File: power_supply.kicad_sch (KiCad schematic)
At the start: 41 parts, among them J1 CONN_01X01, J2 CONN_01X01, J3 CONN_01X01, J4 CONN_01X01, Q1 MMBT42, Q2 FDS2672CT, U1 UCC3803

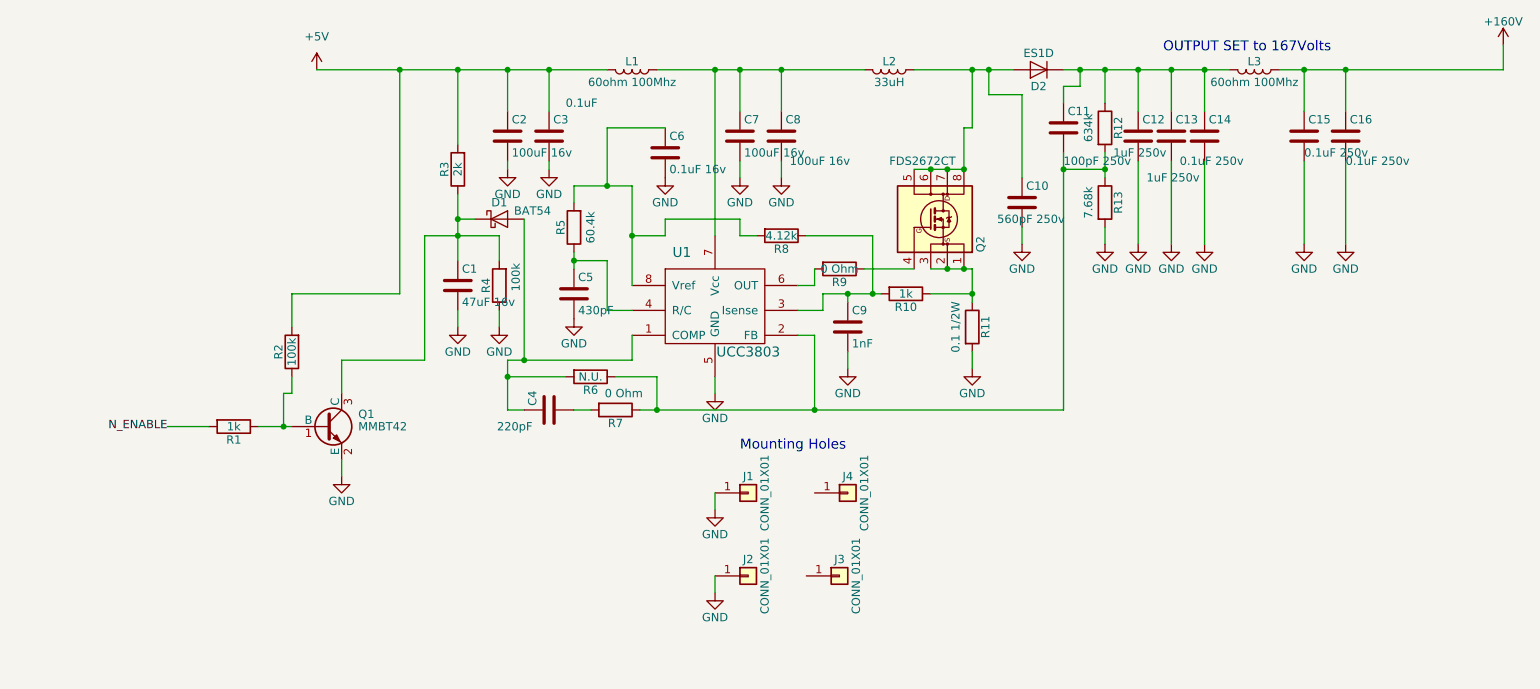
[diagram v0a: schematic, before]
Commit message: Update power supply layout and add associated components
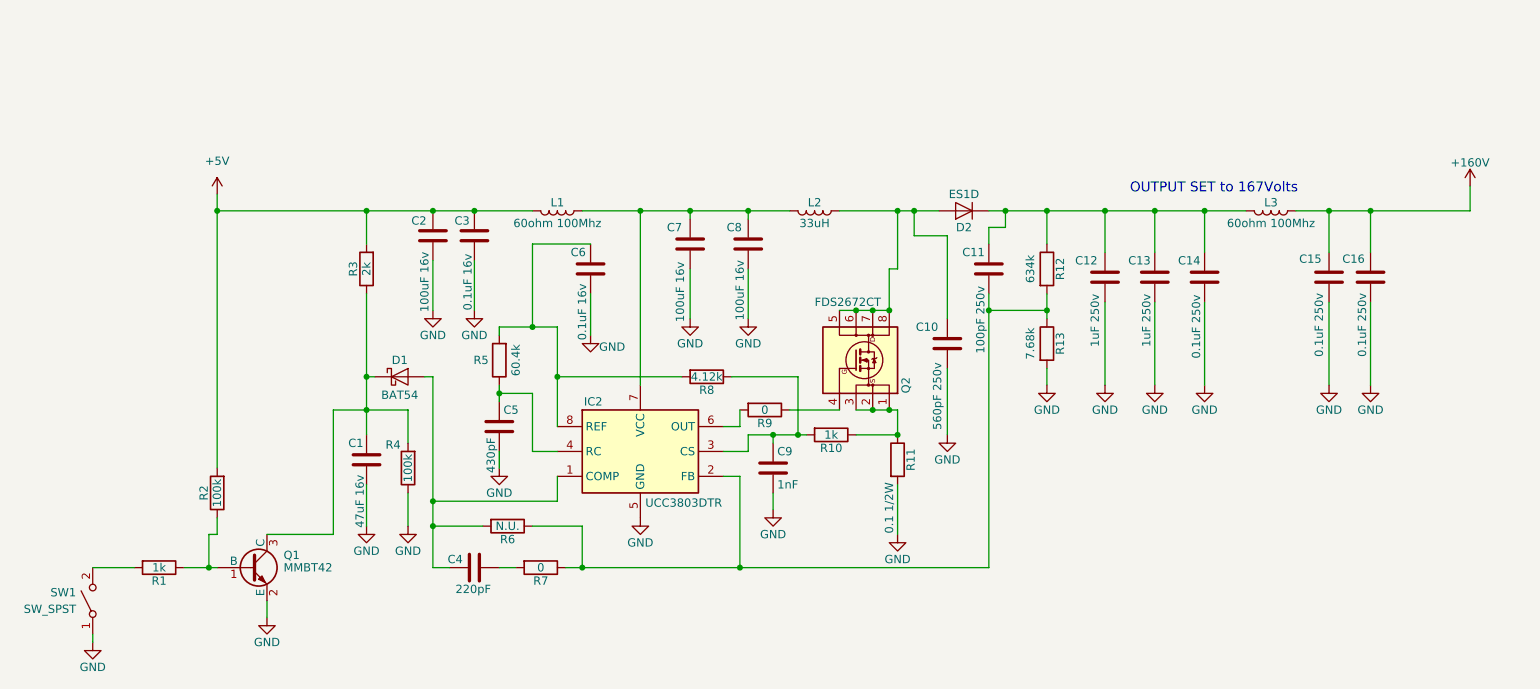
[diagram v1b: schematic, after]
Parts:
- removed J1, J2: CONN_01X01, MountingHole:MountingHole_2.2mm_M2_Pad, symbol NixieSupply5vto160vDCMBoost-rescue:Conn_01x01
- removed J3, J4: CONN_01X01, MountingHole:MountingHole_2.2mm_M2, symbol NixieSupply5vto160vDCMBoost-rescue:Conn_01x01
- removed U1: UCC3803, Package_SO:SOIC-8-1EP_3.9x4.9mm_P1.27mm_EP2.29x3mm, symbol NixieSupply5vto160vDCMBoost-rescue:AAC243
- added IC2: UCC3803DTR, eclectronics_nixie_footprints:SOIC127P600X175-8N, symbol eclectronics_nixie_lib:UCC3803DTR Buck Converter Controller
- added SW1: SW_SPST, symbol Switch:SW_SPST
- C3: value 0.1uF -> 0.1uF 16v
- D1: DigikeyPN (none) -> BAT54HT1GOSCT-ND; LCSCPN (none) -> C7422626; MFN (none) -> onsemi; MPN BAT54WS-7-F -> BAT54HT1G
- D2: DigikeyPN (none) -> ES1DFSCT-ND; MFN (none) -> onsemi
- L1: footprint Resistor_SMD:R_0805_2012Metric_Pad1.20x1.40mm_HandSolder -> Inductor_SMD:L_0805_2012Metric; MFN (none) -> Bourns Inc.; MPN BKP2125HS600-T -> MH2029-600Y
- L2: DigikeyPN (none) -> 732-1244-1-ND; MFN (none) -> Würth Elektronik
- L3: footprint Resistor_SMD:R_0805_2012Metric_Pad1.20x1.40mm_HandSolder -> Inductor_SMD:L_0805_2012Metric; MFN (none) -> Bourns Inc.; MPN (none) -> MH2029-600Y
- R7, R9: value 0 Ohm -> 0
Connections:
- net GND: now also IC2.5 (GND), SW1.1 (A)
- net at C7.1, C8.1, L1.1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: now also IC2.7 (VCC)
- net at C11.2, R12.2, R13.1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: now also IC2.2 (FB)
- net at C5.1, R5.1: now also IC2.4 (RC)
- net at C6.1, R5.2, R8.2: now also IC2.8 (REF)
- net at C9.1, R10.2, R8.1: now also IC2.3 (CS)
- net at C4.1, D1.2 (A), R6.2: now also IC2.1 (COMP)
- net at R9.2: now also IC2.6 (OUT)
- net N_ENABLE: no longer names the net of R1.2
- net N_ENABLE: now also SW1.2 (B)
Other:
- note removed: "Mounting Holes"
- moved on the sheet: C1, C10, C11, C12, C13, C14, C15, C16, C2, C3, C4, C5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

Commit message: Add power supply footprints; begin layout
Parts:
- C1: DigikeyPN (none) -> 445-6003-1-ND; MFN (none) -> TDK; MPN C3216JB1C476M160AB -> C3216X5R1C476M160AB
- C10: DigikeyPN (none) -> 399-C0603C561JAGACTUCT-ND; MFN (none) -> KEMET
- C11: DigikeyPN (none) -> 490-5542-1-ND; MFN (none) -> Murata Electronics; MPN CC0805C101JAGAC7800 -> GRM21A5C2E101JW01D
- C12, C13: DigikeyPN (none) -> 490-3550-1-ND; MFN (none) -> Murata Electronics
- C14, C15, C16: DigikeyPN (none) -> 445-7965-1-ND; MFN (none) -> TDK
- C2, C7, C8: DigikeyPN (none) -> 587-5426-1-ND; MFN (none) -> Taiyo Yuden
- C3: DigikeyPN (none) -> 399-C0603C104K4RACTUCT-ND; MFN (none) -> KEMET; MPN (none) -> C0603C104K4RACTU
- C4: DigikeyPN (none) -> 732-8029-1-ND; MFN (none) -> Würth Elektronik; MPN (none) -> 885012207029
- C5: DigikeyPN (none) -> 311-4238-1-ND; MFN (none) -> YAGEO; MPN CL21C431JBANNNC -> CC0805JRNPO9BN431
- C6: footprint Capacitor_SMD:C_0805_2012Metric_Pad1.18x1.45mm_HandSolder -> Capacitor_SMD:C_0603_1608Metric; DigikeyPN (none) -> 399-C0603C104K4RACTUCT-ND; MFN (none) -> KEMET; MPN (none) -> C0603C104K4RACTU
- C9: DigikeyPN (none) -> 399-C0805C102J5GACTUCT-ND; MFN (none) -> KEMET; MPN (none) -> C0805C102J5GACTU
- Q1: DigikeyPN (none) -> MMBTA42TPMSCT-ND; MFN (none) -> MCC (Micro Commercial Components); MPN (none) -> MMBTA42-TP
- R1: footprint Resistor_SMD:R_0805_2012Metric_Pad1.20x1.40mm_HandSolder -> Resistor_SMD:R_0603_1608Metric; DigikeyPN (none) -> 311-1.00KHRCT-ND; MFN (none) -> YAGEO; MPN (none) -> RC0603FR-071KL
- R10: DigikeyPN (none) -> P1.0KADCT-ND; MFN (none) -> Panasonic Electronic Components; MPN (none) -> ERJ-P06J102V
- R11: DigikeyPN (none) -> P19308CT-ND; MFN (none) -> Panasonic Electronic Components
- R12: DigikeyPN (none) -> 541-634KCCT-ND; MFN (none) -> Vishay Dale; MPN (none) -> CRCW0805634KFKEA
- R13: DigikeyPN (none) -> 311-7.68KFRCT-ND; MFN (none) -> YAGEO; MPN (none) -> RC1206FR-077K68L
- R2, R4: DigikeyPN (none) -> 541-100KCCT-ND; MFN (none) -> Vishay Dale; MPN (none) -> CRCW0805100KFKEA
- R3: DigikeyPN (none) -> 541-2.00KCCT-ND; MFN (none) -> Vishay Dale; MPN (none) -> CRCW08052K00FKEA
- R5: DigikeyPN (none) -> 541-60.4KCCT-ND; MFN (none) -> Vishay Dale; MPN (none) -> CRCW080560K4FKEA
- R7: DigikeyPN (none) -> 311-0.0GRCT-ND; MFN (none) -> YAGEO; MPN (none) -> RC0603JR-070RL
- R8: DigikeyPN (none) -> 541-4.12KCCT-ND; MFN (none) -> Vishay Dale; MPN (none) -> CRCW08054K12FKEA
- R9: footprint Resistor_SMD:R_0805_2012Metric_Pad1.20x1.40mm_HandSolder -> Resistor_SMD:R_0603_1608Metric; DigikeyPN (none) -> 311-0.0GRCT-ND; MFN (none) -> YAGEO; MPN (none) -> RC0603JR-070RL
- SW1: footprint (none) -> Connector_JST:JST_ZH_B2B-ZR-SM4-TF_1x02-1MP_P1.50mm_Vertical

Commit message: Add DigiKey part numbers to components
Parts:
- L1: DigikeyPN (none) -> MH2029-600YCT-ND
- L3: DigiKeyPN (none) -> MH2029-600YCT-ND; DigikeyPN (none) -> MH2029-600YCT-ND
